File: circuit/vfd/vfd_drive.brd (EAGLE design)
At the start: 100 x 100 mm, 55 parts, among them J1 ZX62R-AB-5P, J2 DC_JACK_2DC0005D100, J3 PSM-210223-10, J4 PSM-210223-10, J5 FSM-21045-10, J6 FSM-21045-10, J7 PSM-210223-8, J8 FSM-21045-8, Q1 FA-238V, SW1 SKRPACE010, SW2 SKRPACE010, U1 PIC18F14K50-I, U2 MAX6921AWI+, U3 NJW4131, U4 DS3231M, U5 ADP3338AKCZ-3.3, U9 BME280

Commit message: [add]add all as backup
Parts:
- added U6: PSF-A85, ITEAD:PSF-A85
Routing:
- net N$9: track 19.8 -> 7.08 mm
- net N$10: track 15.8 -> 3.67 mm
- net N$8: track 19.8 -> 7.99 mm
- net N$11: track 16.7 -> 5.24 mm
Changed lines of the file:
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@@
 <hole x="25" y="59.5" drill="3.2"/>
 <circle x="25" y="59.5" radius="3" width="0.0762" layer="47"/>
+<dimension x1="25" y1="93.5" x2="25" y2="56.5" x3="-7" y3="75" textsize="1.778" layer="1"/>
 </plain>
 <attributes>
@@
 <attribute name="NAME" x="34.382" y="71.929" size="1.27" layer="25" rot="R270"/>
 </element>
+<element name="U6" library="ITEAD" package="PSF-A85" value="PSF-A85" x="9.5" y="71.5" smashed="yes">
+<attribute name="NAME" x="14.072" y="80.644" size="1.27" layer="25"/>
+<attribute name="VALUE" x="14.072" y="78.612" size="1.27" layer="27"/>
+</element>
 </elements>
 <signals>
@@
 <wire x1="21" y1="86.5" x2="20.5" y2="87" width="0.1524" layer="1"/>
 <wire x1="20.5" y1="87" x2="20.5" y2="88.325" width="0.1524" layer="1"/>
-<wire x1="30.885" y1="78.115" x2="22.5" y2="86.5" width="0.1524" layer="1"/>
 <contactref element="U1" pad="6"/>
 <wire x1="33.625" y1="75.665" x2="32.135" y2="75.665" width="0.1524" layer="1"/>
 <wire x1="30.885" y1="76.915" x2="30.885" y2="78.115" width="0.1524" layer="1"/>
 <wire x1="32.135" y1="75.665" x2="30.885" y2="76.915" width="0.1524" layer="1"/>
+<wire x1="30.885" y1="78.115" x2="22.5" y2="86.5" width="0" layer="19" extent="1-1"/>
 </signal>
 <signal name="N$9">
 <contactref element="J8" pad="6"/>
 <contactref element="U1" pad="7"/>
-<wire x1="22.5" y1="87.5" x2="31.5" y2="78.5" width="0.1524" layer="1"/>
 <wire x1="31.5" y1="78.5" x2="31.5" y2="77" width="0.1524" layer="1"/>
 <wire x1="31.5" y1="77" x2="32.185" y2="76.315" width="0.1524" layer="1"/>
 <wire x1="32.185" y1="76.315" x2="33.625" y2="76.315" width="0.1524" layer="1"/>
 <wire x1="22.5" y1="90.675" x2="22.5" y2="87.5" width="0.1524" layer="1"/>
+<wire x1="22.5" y1="87.5" x2="31.5" y2="78.5" width="0" layer="19" extent="1-1"/>
 </signal>
 <signal name="N$10">
@@
 <contactref element="U1" pad="8"/>
 <wire x1="24.5" y1="88.325" x2="24.5" y2="86.5" width="0.1524" layer="1"/>
-<wire x1="24.5" y1="86.5" x2="32" y2="79" width="0.1524" layer="1"/>
-<wire x1="32" y1="79" x2="32" y2="77.5" width="0.1524" layer="1"/>
 <wire x1="32" y1="77.5" x2="32.535" y2="76.965" width="0.1524" layer="1"/>
 <wire x1="32.535" y1="76.965" x2="33.625" y2="76.965" width="0.1524" layer="1"/>
+<wire x1="32" y1="77.5" x2="24.5" y2="86.5" width="0" layer="19" extent="1-1"/>
 </signal>
 <signal name="N$11">
 <contactref element="J8" pad="4"/>
 <contactref element="U1" pad="9"/>
-<wire x1="33.625" y1="77.615" x2="32.515" y2="77.615" width="0.1524" layer="1"/>
-<wire x1="32.515" y1="77.615" x2="32.44" y2="77.69" width="0.1524" layer="1"/>
-<wire x1="32.44" y1="77.69" x2="32.44" y2="79.49" width="0.1524" layer="1"/>
 <wire x1="26.5" y1="85.43" x2="26.5" y2="90.675" width="0.1524" layer="1"/>
-<wire x1="32.44" y1="79.49" x2="26.5" y2="85.43" width="0.1524" layer="1"/>
+<wire x1="26.5" y1="85.43" x2="33.625" y2="77.615" width="0" layer="19" extent="1-1"/>
 </signal>
 </signals>

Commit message: [tem@]
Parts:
- removed C12: 10uF, taki-library:C3216
- removed J3, J4: PSM-210223-10, taki-library:PSM-210223-10
- removed J5, J6: FSM-21045-10, taki-library:FSM-21045-10
- removed J7: PSM-210223-8, taki-library:PSM-210223-8
- added R11: 27k, taki-library:R0603
- C2: value 0.1uF -> 10uF; device taki-library:C0603 -> taki-library:C3216
- moved J2 143.1 mm to (134.0, -62.5)
- moved BATT1 133.2 mm to (-0.99, -37.2)
- moved C1 133.2 mm to (42.0, -97.5)
- moved C10 133.2 mm to (60.0, -15.9)
- moved C16 133.2 mm to (60.2, -60.2)
- moved C18 133.2 mm to (44.1, -68.2)
- moved C19 133.2 mm to (40.9, -67.2)
- moved C22 133.2 mm to (43.0, -64.3)
- moved C3 133.2 mm to (67.9, -58.6)
- moved C4 133.2 mm to (67.9, -56.4)
- moved C7 133.2 mm to (53.7, -18.9)
- moved C8 133.2 mm to (50.4, -16.6)
- moved J1 133.2 mm to (63.0, -67.2)
- moved J8 133.2 mm to (59.0, -41.0)
- moved LED3 133.2 mm to (26.4, -13.7)
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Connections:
- removed net N$21: J5.3, U2.26
- removed net N$22: J5.4, U2.25
- removed net N$23: J5.5, U2.24
- removed net N$24: J5.6, U2.23
- removed net N$25: J5.7, U2.22
- removed net N$26: J5.8, U2.21
- removed net N$27: J5.9, U2.20
- removed net N$28: J5.10, U2.19
- removed net N$29: J6.2, U2.18
- removed net N$30: J6.7, U2.9
- removed net N$31: J6.8, U2.10
- removed net N$32: J6.9, U2.11
- removed net N$33: J6.10, U2.12
- removed net N$34: J6.3, U2.17
- removed net N$35: J6.6, U2.8
- removed net N$36: J6.5, U2.7
- removed net N$37: J6.4, U2.6
- removed net N$38: J5.2, J7.2
- removed net N$7: J7.7, U2.13
- net +24V: now also C2.1, U2.1; no longer C12.1
- net +5V: now also R11.2
- net GND: no longer C12.2, J3.1, J4.1, J5.1, J6.1, J7.8, U2.14
- net N$1: now also R11.1, U3.2; no longer J7.1, U2.1
- net N$2: no longer J7.3
- net N$3: no longer J7.4
- net N$39: no longer C2.1
- net N$4: no longer J7.5
- net N$5: no longer J7.6
- net VBIAS: no longer J4.2
- net VFD10: now also U2.22; no longer J4.4
- net VFD11: now also U2.21; no longer J4.5
- net VFD12: now also U2.20; no longer J4.6
- net VFD14: now also U2.19; no longer J4.7
- net VFD15: now also U2.18; no longer J4.8
- net VFD16: now also U2.17; no longer J4.9
- net VFD17: now also U2.7; no longer J4.10
- net VFD18: now also U2.8; no longer J3.10
- net VFD19: now also U2.9; no longer J3.9
- net VFD2: now also U2.6; no longer J3.5
- net VFD20: now also U2.10; no longer J3.8
- net VFD21: now also U2.11; no longer J3.7
- net VFD22: now also U2.12; no longer J3.6
- net VFD3: now also U2.26; no longer J3.4
- net VFD4: now also U2.25; no longer J3.3
- net VFD5: now also U2.24; no longer J3.2
- net VFD9: now also U2.23; no longer J4.3
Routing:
- net GND: track 209.8 -> 121.8 mm, vias 6 -> 0
- net VFD22: track 8.39 -> 51.5 mm
- net VFD21: track 6.84 -> 49.3 mm
- net VFD20: track 10.3 -> 47.7 mm
- net VFD19: track 9.47 -> 45.0 mm
- net +5V: track 41.1 -> 10.5 mm
- net VFD17: track 10.8 -> 40.7 mm
- net N$4: track 28.8 -> 0.00 mm, vias 3 -> 0
- net VFD18: track 14.8 -> 43.0 mm
- net N$7: track 26.5 -> 0.00 mm, vias 1 -> 0
- net +24V: track 32.1 -> 58.4 mm
- net N$5: track 25.9 -> 0.00 mm, vias 1 -> 0
- net N$29: track 23.9 -> 0.00 mm, vias 2 -> 0
- net N$34: track 21.3 -> 0.00 mm, vias 2 -> 0
- net N$1: track 21.8 -> 1.72 mm, vias 3 -> 0
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- added copper zone on layer 1, net N$41
- removed copper zone on layer 16, net GND
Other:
- board size 100 x 100 mm -> 46 x 46 mm

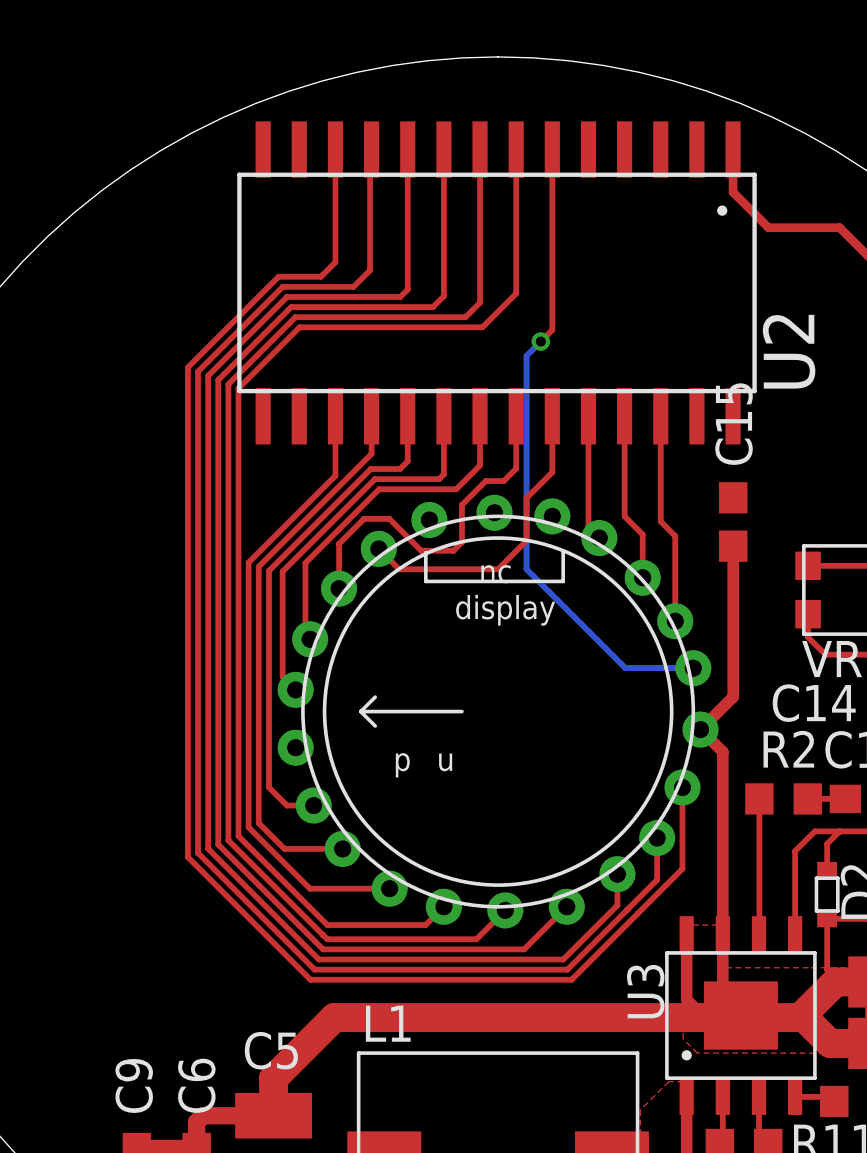
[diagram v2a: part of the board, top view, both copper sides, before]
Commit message: [fix]fix decimal point anode route
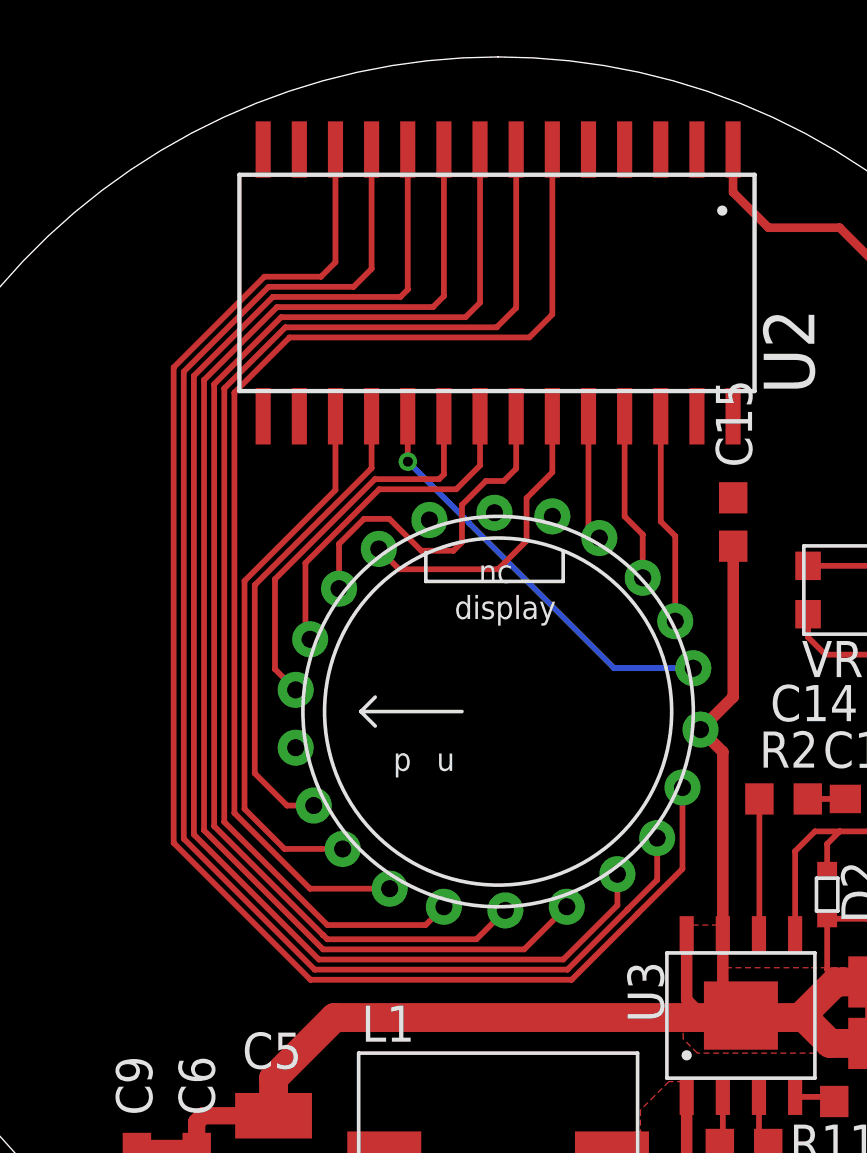
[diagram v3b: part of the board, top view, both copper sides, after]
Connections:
- net VFD14: now also U2.18; no longer U2.19
- net VFD15: now also U2.17; no longer U2.18
- net VFD16: now also U2.6; no longer U2.17
- net VFD2: now also U2.19; no longer U2.6
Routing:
- net VFD16: track 21.6 -> 39.4 mm
- net VFD2: track 22.4 -> 14.6 mm
- net VFD17: track 40.7 -> 41.7 mm
- net VFD14: track 17.5 -> 16.8 mm
- net VFD18: track 43.0 -> 43.7 mm
- net VFD22: track 51.5 -> 52.2 mm
- net VFD20: track 47.7 -> 48.4 mm
- net VFD19: track 45.0 -> 45.7 mm
- net VFD21: track 49.3 -> 50.0 mm
